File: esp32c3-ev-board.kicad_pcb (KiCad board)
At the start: 4 copper layers, 51 x 60 mm, 65 parts, among them IC1 SPX3819M5-L-3-3, IC2 ACS711EEXTK-31AB-T, IC3 ESP32-C3FH4, IC4 W25Q128JVSIQ, J2 DC Connecter, J4 Conn_01x04_Pin, J5 USB_C_Receptacle_USB2.0, J6 Screw_Terminal_01x03, SW2 SW_DPST_x2, SW3 SW_DPST_x2, U1 USBLC6-2SC6, U2 USBLC6-2SC6, Y1 40MHZ

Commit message: finished outline
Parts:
- moved ANT1 4.21 mm to (135.6, 115.4)
- moved C7 2.86 mm to (136.1, 99.8)
- moved C9 2.86 mm to (136.4, 104.4)
- moved IC3 2.86 mm to (131.2, 102.4)
- moved C10 2.86 mm to (126.8, 105.1)
- moved C11 2.86 mm to (134.7, 98.2)
- moved C19 2.86 mm to (136.5, 87.3)
- moved C20 2.86 mm to (134.2, 87.3)
- moved IC4 2.86 mm to (130.0, 87.9)
- moved R12 2.86 mm to (121.8, 104.5)
- moved C12 2.44 mm to (133.1, 114.5)
- moved C14 2.44 mm to (136.5, 111.5)
- moved C15 2.44 mm to (128.7, 114.2)
- moved C8 2.44 mm to (125.0, 111.5)
- moved L2 2.44 mm to (132.3, 111.4)
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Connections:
- ANT1 pad 1: Reg Neg -> Net-(ANT1-Pad1)
- ANT1 pad 2: Net-(ANT1-Pad2) -> Reg Neg
- C15 pad 1: Net-(ANT1-Pad2) -> Net-(ANT1-Pad1)
- L3 pad 1: Net-(ANT1-Pad2) -> Net-(ANT1-Pad1)
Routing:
- net Net-(IC3-XTAL_N): track 19.8 -> 17.3 mm
- net Net-(C21-Pad1): track 12.1 -> 9.70 mm
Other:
- board size 51 x 60 mm -> 51 x 66.7 mm
- board text added: "(43/2)-(15.2/2) = 13.9"
- board text added: "d1+l3+l5+l2+l5+l2+d3 = 0.5+5+2+2.7+2+2.7+0.3 = 15.2"

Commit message: Almost finished
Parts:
- removed the SW2 at (146.1, 60.1)
- added H5: MountingHole_Pad, MountingHole:MountingHole_2.7mm_M2.5_Pad, F.Cu at (112.0, 82.5)
- added H6: MountingHole_Pad, MountingHole:MountingHole_2.7mm_M2.5_Pad, F.Cu at (112.1, 72.2)
- added IC5: AH1390-HK4-7, AH1390-HK4-7:AH1390HK47, F.Cu at (149.8, 121.9)
- added J7: Conn_01x04_Pin, Connector_PinHeader_2.54mm:PinHeader_1x04_P2.54mm_Vertical, F.Cu at (146.0, 118.8)
- added J9: Battery Neg(Series), Connector_PinSocket_2.54mm:PinSocket_1x02_P2.54mm_Vertical, F.Cu at (157.1, 104.9)
- added R17: 1k, Resistor_SMD:R_0805_2012Metric_Pad1.20x1.40mm_HandSolder, F.Cu at (153.2, 105.0)
- added SW1: SW_DPST_x2, SKRPANE010:SKRPADE010, F.Cu at (146.1, 60.0)
- moved R3 15.9 mm to (123.0, 69.3)
- moved R2 15.9 mm to (118.2, 69.3)
- moved C12 6.83 mm to (133.4, 107.6)
- moved U1 6.25 mm to (133.1, 68.2)
- moved C13 5.41 mm to (133.5, 114.0)
- moved C23 5.04 mm to (115.0, 93.0), turned to -90 degrees
- moved R16 4.80 mm to (152.7, 97.0)
- moved R8 4.11 mm to (140.8, 102.9)
- moved J6 3.04 mm to (157.1, 96.1)
- moved C1 2.99 mm to (121.3, 78.9)
- moved IC2 2.99 mm to (116.3, 77.4)
- moved R1 2.99 mm to (121.3, 75.2)
- moved C19 2.96 mm to (137.5, 90.1)
- moved IC4 2.96 mm to (131.0, 90.7)
- moved C20 2.96 mm to (135.2, 90.1)
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- renumbered SW3 to SW2
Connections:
- net USBDN renamed USBD-
- net USBDP renamed USBD+
- H2 pad 1: Reg Neg -> UnregPos
- IC3 pad 12: unconnected-(IC3-MTCK-Pad12) -> LED B
- IC3 pad 9: LED B -> Net-(IC3-MTMS)
- J4 pad 1: VBUS -> Net-(J4-Pin_1)
- J4 pad 2: Net-(J4-Pin_2) -> VBUS
- J6 pad 2: Reg Neg -> Net-(IC3-MTDI)
- J6 pad 3: Net-(IC3-MTDI) -> Reg Neg
- R12 pad 1: Net-(C21-Pad1) -> Net-(IC3-XTAL_P)
- R12 pad 2: Net-(IC3-XTAL_P) -> Net-(C21-Pad1)
- SW2 pad 2: GND -> CHIPEN
- SW2 pad 3: (no net) -> Reg Neg
- SW2 pad 4: (no net) -> Reg Neg
- U2 pad 4: Net-(J4-Pin_2) -> Net-(J4-Pin_1)
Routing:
- net +3.3V: track 5.52 -> 230.1 mm, vias 0 -> 14
- net CurMeas: track 9.49 -> 88.4 mm, vias 0 -> 5
- net CHIPEN: track 9.33 -> 65.9 mm, vias 0 -> 2
- net VoltMeas: track 0.00 -> 52.8 mm, vias 0 -> 2
- net Reg Neg: track 0.00 -> 40.7 mm, vias 0 -> 35
- net USBD-: track 0.00 -> 37.7 mm
- net USBD+: track 0.00 -> 37.6 mm
- net Net-(IC3-MTDI): track 0.00 -> 27.5 mm, vias 0 -> 2
- net Net-(IC3-MTMS): track 0.00 -> 26.5 mm, vias 0 -> 2
- net Net-(IC3-GPIO2): track 0.00 -> 21.0 mm, vias 0 -> 2
- net LED B: track 0.00 -> 19.7 mm, vias 0 -> 2
- net Net-(IC3-SPICS0): track 0.97 -> 19.2 mm, vias 0 -> 2
- net Net-(IC3-SPIWP): track 0.94 -> 16.9 mm, vias 0 -> 2
- net LED A: track 0.00 -> 14.0 mm
- net Net-(IC3-U0TXD): track 0.00 -> 13.5 mm
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- added copper zone on B.Cu, net +3.3V
- added copper zone on B.Cu, net Reg Neg
- added copper zone on F.Cu, net Reg Neg
- added copper zone on In1.Cu, net Reg Neg
- added copper zone on In2.Cu, net Reg Neg
- added copper zone on B.Cu, net UnregNeg(furthest from bat term)
- added copper zone on F.Cu, net UnregNeg(furthest from bat term)
- added copper zone on In1.Cu, net UnregNeg(furthest from bat term)
- added copper zone on In2.Cu, net UnregNeg(furthest from bat term)
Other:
- outline, holes or cut-outs redrawn

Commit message: finishing touches
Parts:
- removed C15, C16: 3p3, Capacitor_SMD:C_0603_1608Metric_Pad1.08x0.95mm_HandSolder
- added H7: MountingHole_Pad, MountingHole:MountingHole_2.2mm_M2, F.Cu at (128.1, 80.8)
- Negative +: renamed from H6
- Negative -: renamed from H5
- moved L3 1.23 mm to (129.6, 110.2)
- moved C10 0.40 mm to (126.8, 105.5)
- turned R12 to -90 degrees
- renumbered D3 to A, D6 to B, SW1 to B, IC4 to Flash, J6 to Hall, J7 to Hall, H2 to Positive, SW2 to R, IC1 to Reg, J9 to Therm, J4 to UART
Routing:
- net Reg Neg: track 40.7 -> 54.3 mm, vias 35 -> 58
- net Net-(ANT1-Pad1): track 0.00 -> 6.80 mm
- net +3.3V: track 230.1 -> 235.3 mm, vias 14 -> 13
- net Net-(IC3-LNA_IN): track 0.00 -> 4.17 mm
- net 5vUSB: track 18.4 -> 21.7 mm
- net Net-(J5-D+-PadA6): track 2.37 -> 4.82 mm
- net Net-(IC3-SPICS0): track 19.2 -> 18.0 mm
- net CHIPEN: vias 2 -> 3
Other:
- outline, holes or cut-outs redrawn
- board text added: "- +"
- board text added: "EvoMon Version 1.1 Jai and Alex"

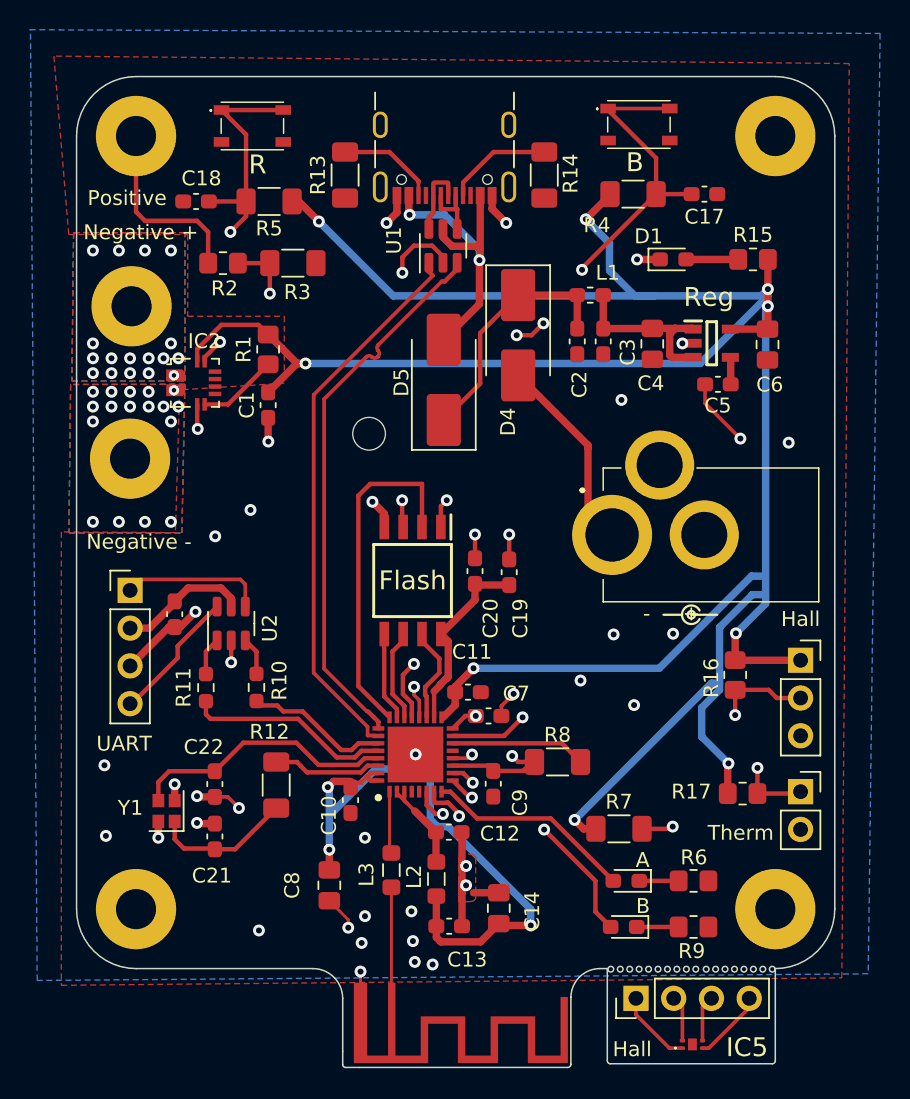
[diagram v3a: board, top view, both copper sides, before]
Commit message: PCBWAY VER || SWITCHING TO JLC
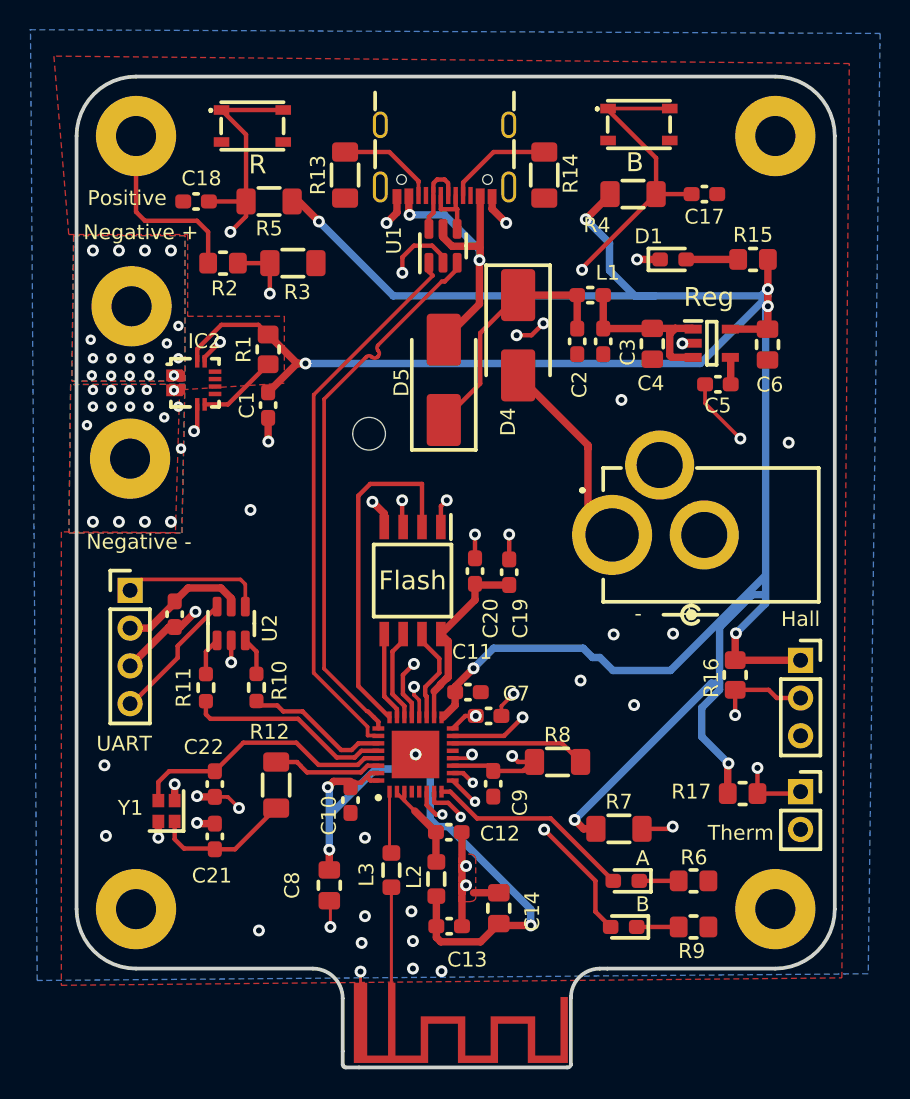
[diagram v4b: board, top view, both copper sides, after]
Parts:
- removed the Hall at (146.0, 118.8)
- removed IC5: AH1390-HK4-7, AH1390-HK4-7:AH1390HK47
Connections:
- J5 pad A12: (no net) -> Reg Neg
- J5 pad B1: (no net) -> Reg Neg
- J5 pad B12: (no net) -> Reg Neg
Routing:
- net Net-(IC5-VDD): track 5.16 -> 0.00 mm
- net Net-(IC5-GND): track 4.90 -> 0.00 mm
- net Net-(IC5-OUTPUT_2_(SOUTH-_POLE)): track 3.10 -> 0.00 mm
- net Net-(IC5-OUTPUT_1_(NORTH_-POLE): track 3.09 -> 0.00 mm
- net +3.3V: track 235.3 -> 236.5 mm
- net CHIPEN: track 65.9 -> 65.8 mm, vias 3 -> 2
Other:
- outline, holes or cut-outs redrawn
- board text added: "Designed and built by: Jai Nielsen and Alex McAuley"
- board text added: "EvoMon REV 2"
- board text removed: "EvoMon Version 1.1 Jai and Alex"

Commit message: ordered board
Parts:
- moved L2 0.31 mm to (132.9, 110.8)
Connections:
- J2 pad 3: (no net) -> Reg Neg
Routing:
- net Reg Neg: track 54.0 -> 71.6 mm, vias 58 -> 61
- net USBD-: track 37.7 -> 40.1 mm
- net USBD+: track 37.6 -> 39.7 mm
